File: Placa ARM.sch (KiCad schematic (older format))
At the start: 0 parts

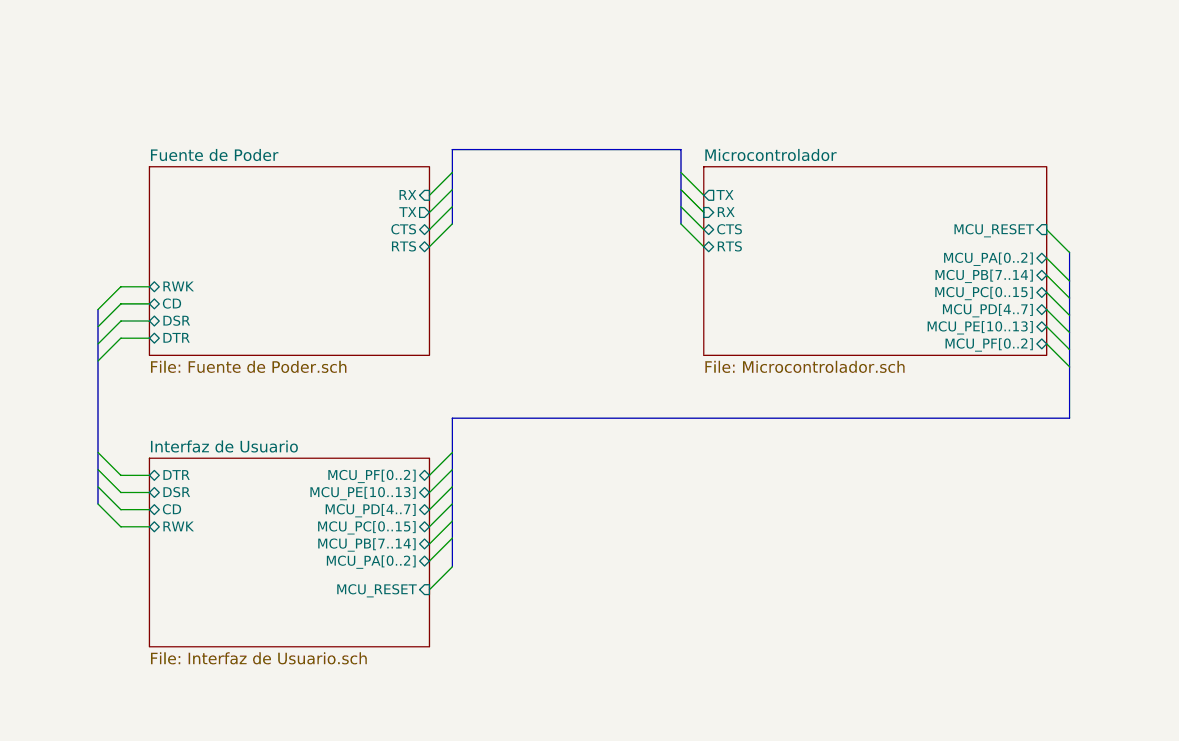
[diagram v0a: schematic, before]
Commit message: Issue #1: Correción de las conexiones Bus
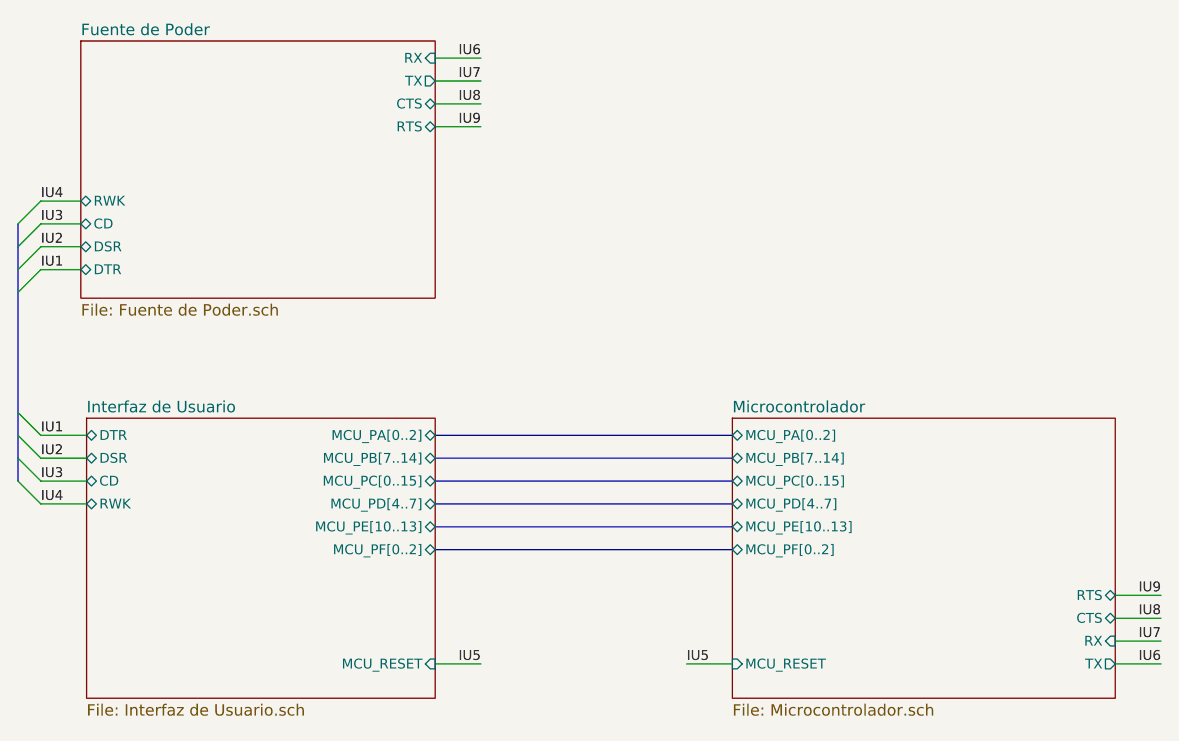
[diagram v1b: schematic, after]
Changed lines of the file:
@@
 $EndDescr
 $Sheet
-S 3950 2700 1225 825
+S 3650 2150 1550 1125
 U 5F4D2198
 F0 "Fuente de Poder" 50
 F1 "Fuente de Poder.sch" 50
-F2 "RX" I R 5175 2825 43
-F3 "TX" O R 5175 2900 43
-F4 "RWK" B L 3950 3225 43
-F5 "CD" B L 3950 3300 43
-F6 "DSR" B L 3950 3375 43
-F7 "DTR" B L 3950 3450 43
-F8 "CTS" B R 5175 2975 43
-F9 "RTS" B R 5175 3050 43
+F2 "RX" I R 5200 2225 43
+F3 "TX" O R 5200 2325 43
+F4 "RWK" B L 3650 2850 43
+F5 "CD" B L 3650 2950 43
+F6 "DSR" B L 3650 3050 43
+F7 "DTR" B L 3650 3150 43
+F8 "CTS" B R 5200 2425 43
+F9 "RTS" B R 5200 2525 43
 $EndSheet
 $Sheet
-S 3950 3975 1225 825
+S 3675 3800 1525 1225
 U 5F4D946F
 F0 "Interfaz de Usuario" 50
 F1 "Interfaz de Usuario.sch" 50
-F2 "RWK" B L 3950 4275 43
-F3 "DTR" B L 3950 4050 43
-F4 "DSR" B L 3950 4125 43
-F5 "CD" B L 3950 4200 43
-F6 "MCU_PA[0..2]" B R 5175 4425 43
-F7 "MCU_PB[7..14]" B R 5175 4350 43
-F8 "MCU_PE[10..13]" B R 5175 4125 43
-F9 "MCU_PC[0..15]" B R 5175 4275 43
-F10 "MCU_PD[4..7]" B R 5175 4200 43
-F11 "MCU_PF[0..2]" B R 5175 4050 43
-F12 "MCU_RESET" I R 5175 4550 43
+F2 "RWK" B L 3675 4175 43
+F3 "DTR" B L 3675 3875 43
+F4 "DSR" B L 3675 3975 43
+F5 "CD" B L 3675 4075 43
+F6 "MCU_PA[0..2]" B R 5200 3875 43
+F7 "MCU_PB[7..14]" B R 5200 3975 43
+F8 "MCU_PE[10..13]" B R 5200 4275 43
+F9 "MCU_PC[0..15]" B R 5200 4075 43
+F10 "MCU_PD[4..7]" B R 5200 4175 43
+F11 "MCU_PF[0..2]" B R 5200 4375 43
+F12 "MCU_RESET" I R 5200 4875 43
 $EndSheet
 $Sheet
-S 6375 2700 1500 825
+S 6500 3800 1675 1225
 U 5F4D1FFB
 F0 "Microcontrolador" 50
 F1 "Microcontrolador.sch" 50
-F2 "MCU_PA[0..2]" B R 7875 3100 43
-F3 "MCU_PB[7..14]" B R 7875 3175 43
-F4 "MCU_PE[10..13]" B R 7875 3400 43
-F5 "MCU_PC[0..15]" B R 7875 3250 43
-F6 "MCU_PD[4..7]" B R 7875 3325 43
-F7 "RX" I L 6375 2900 43
-F8 "TX" O L 6375 2825 43
-F9 "CTS" B L 6375 2975 43
-F10 "RTS" B L 6375 3050 43
-F11 "MCU_PF[0..2]" B R 7875 3475 43
-F12 "MCU_RESET" I R 7875 2975 43
+F2 "MCU_PA[0..2]" B L 6500 3875 43
+F3 "MCU_PB[7..14]" B L 6500 3975 43
+F4 "MCU_PE[10..13]" B L 6500 4275 43
+F5 "MCU_PC[0..15]" B L 6500 4075 43
+F6 "MCU_PD[4..7]" B L 6500 4175 43
+F7 "RX" I R 8175 4775 43
+F8 "TX" O R 8175 4875 43
+F9 "CTS" B R 8175 4675 43
+F10 "RTS" B R 8175 4575 43
+F11 "MCU_PF[0..2]" B L 6500 4375 43
+F12 "MCU_RESET" I L 6500 4875 43
 $EndSheet
 Entry Wire Line
-	3725 3325 3825 3225
+	3375 3150 3475 3050
 Entry Wire Line
-	3725 3400 3825 3300
+	3375 2950 3475 2850
 Entry Wire Line
-	3725 3475 3825 3375
+	3375 3250 3475 3150
 Entry Wire Line
-	3725 3550 3825 3450
+	3375 3050 3475 2950
 Entry Wire Line
-	3725 3950 3825 4050
+	3375 3775 3475 3875
 Entry Wire Line
-	3725 4025 3825 4125
+	3375 3875 3475 3975
 Entry Wire Line
-	3725 4100 3825 4200
+	3375 3975 3475 4075
 Entry Wire Line
-	3725 4175 3825 4275
+	3375 4075 3475 4175
+Text Label 3475 3150 0    43   ~ 0
+IU1
+Text Label 3475 3975 0    43   ~ 0
+IU2
+Text Label 3475 4075 0    43   ~ 0
+IU3
+Text Label 3475 4175 0    43   ~ 0
+IU4
+Text Label 3475 3050 0    43   ~ 0
+IU2
+Text Label 3475 2950 0    43   ~ 0
+IU3
+Text Label 3475 3875 0    43   ~ 0
+IU1
 Wire Wire Line
-	3825 4050 3950 4050
+	3675 3875 3475 3875
 Wire Wire Line
-	3825 4125 3950 4125
+	3675 3975 3475 3975
 Wire Wire Line
-	3825 4200 3950 4200
+	3675 4075 3475 4075
 Wire Wire Line
-	3825 4275 3950 4275
+	3675 4175 3475 4175
 Wire Wire Line
-	3825 3225 3950 3225
+	3475 2850 3650 2850
 Wire Wire Line
-	3825 3300 3950 3300
+	3475 2950 3650 2950
 Wire Wire Line
-	3825 3375 3950 3375
+	3475 3050 3650 3050
 Wire Wire Line
-	3825 3450 3950 3450
-Entry Wire Line
-	6275 2725 6375 2825
-Entry Wire Line
-	6275 2800 6375 2900
-Entry Wire Line
-	6275 2875 6375 2975
-Entry Wire Line
-	6275 2950 6375 3050
-Entry Wire Line
-	5175 2825 5275 2725
-Entry Wire Line
-	5175 2900 5275 2800
-Entry Wire Line
-	5175 2975 5275 2875
-Entry Wire Line
-	5175 3050 5275 2950
+	3475 3150 3650 3150
+Text Label 3475 2850 0    43   ~ 0
+IU4
+Wire Wire Line
+	5200 4875 5400 4875
+Text Label 5400 4875 2    43   ~ 0
+IU5
+Wire Wire Line
+	6500 4875 6300 4875
+Text Label 6300 4875 0    43   ~ 0
+IU5
+Wire Wire Line
+	5200 2225 5400 2225
+Wire Wire Line
+	5200 2325 5400 2325
+Wire Wire Line
+	5200 2425 5400 2425
+Wire Wire Line
+	5200 2525 5400 2525
+Text Label 5400 2225 2    43   ~ 0
+IU6
+Text Label 5400 2325 2    43   ~ 0
+IU7
+Text Label 5400 2425 2    43   ~ 0
+IU8
+Text Label 5400 2525 2    43   ~ 0
+IU9
+Wire Wire Line
+	8175 4575 8375 4575
+Wire Wire Line
+	8175 4675 8375 4675
+Wire Wire Line
+	8175 4775 8375 4775
+Wire Wire Line
+	8175 4875 8375 4875
+Text Label 8375 4775 2    43   ~ 0
+IU7
+Text Label 8375 4675 2    43   ~ 0
+IU8
+Text Label 8375 4575 2    43   ~ 0
+IU9
+Text Label 8375 4875 2    43   ~ 0
+IU6
 Wire Bus Line
-	6275 2625 5275 2625
-Entry Wire Line
-	5175 4050 5275 3950
-Entry Wire Line
-	5175 4125 5275 4025
-Entry Wire Line
-	5175 4200 5275 4100
-Entry Wire Line
-	5175 4275 5275 4175
-Entry Wire Line
-	5175 4350 5275 4250
-Entry Wire Line
-	5175 4425 5275 4325
-Entry Wire Line
-	7875 3100 7975 3200
-Entry Wire Line
-	7875 3175 7975 3275
-Entry Wire Line
-	7875 3250 7975 3350
-Entry Wire Line
-	7875 3325 7975 3425
-Entry Wire Line
-	7875 3400 7975 3500
-Entry Wire Line
-	7875 3475 7975 3575
+	5200 3875 6500 3875
 Wire Bus Line
-	7975 3800 5275 3800
-Entry Wire Line
-	7875 2975 7975 3075
-Entry Wire Line
-	5175 4550 5275 4450
+	6500 3975 5200 3975
 Wire Bus Line
-	6275 2625 6275 2950
+	5200 4075 6500 4075
 Wire Bus Line
-	5275 2625 5275 2950
+	6500 4175 5200 4175
 Wire Bus Line
-	3725 3325 3725 4175
+	5200 4275 6500 4275
 Wire Bus Line
-	5275 3800 5275 4450
+	6500 4375 5200 4375
 Wire Bus Line
-	7975 3075 7975 3800
+	3375 2950 3375 4075
 $EndSCHEMATC

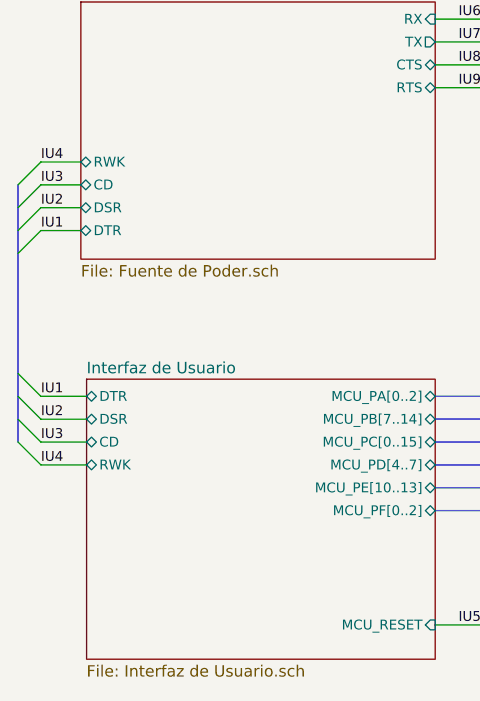
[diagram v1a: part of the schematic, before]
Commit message: Issue #1: Cambio de conector USB-UART
Se agrega un conector para todos los pines UART ofrecidos por el IC
XR21B1411 de Maxlinear.
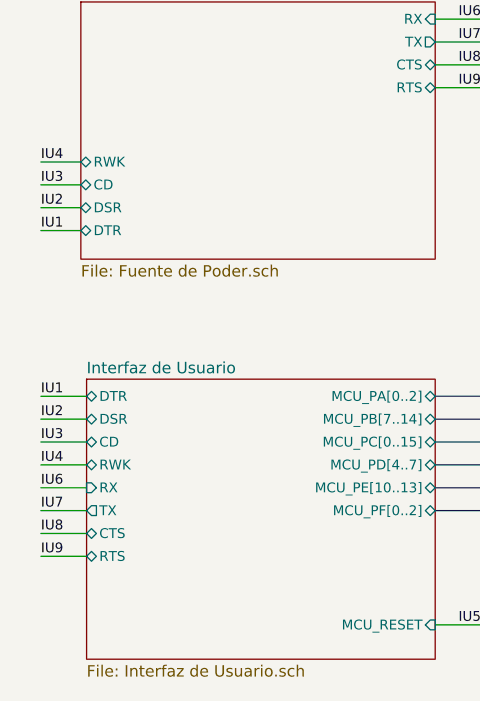
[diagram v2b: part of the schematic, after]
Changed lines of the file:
@@
 F11 "MCU_PF[0..2]" B R 5200 4375 43
 F12 "MCU_RESET" I R 5200 4875 43
+F13 "RX" I L 3675 4275 43
+F14 "TX" O L 3675 4375 43
+F15 "CTS" B L 3675 4475 43
+F16 "RTS" B L 3675 4575 43
 $EndSheet
 $Sheet
@@
 F12 "MCU_RESET" I L 6500 4875 43
 $EndSheet
-Entry Wire Line
-	3375 3150 3475 3050
-Entry Wire Line
-	3375 2950 3475 2850
-Entry Wire Line
-	3375 3250 3475 3150
-Entry Wire Line
-	3375 3050 3475 2950
-Entry Wire Line
-	3375 3775 3475 3875
-Entry Wire Line
-	3375 3875 3475 3975
-Entry Wire Line
-	3375 3975 3475 4075
-Entry Wire Line
-	3375 4075 3475 4175
 Text Label 3475 3150 0    43   ~ 0
 IU1
@@
 Wire Bus Line
 	6500 4375 5200 4375
-Wire Bus Line
-	3375 2950 3375 4075
+Wire Wire Line
+	3675 4275 3475 4275
+Wire Wire Line
+	3675 4375 3475 4375
+Wire Wire Line
+	3675 4475 3475 4475
+Wire Wire Line
+	3675 4575 3475 4575
+Text Label 3475 4275 0    43   ~ 0
+IU6
+Text Label 3475 4375 0    43   ~ 0
+IU7
+Text Label 3475 4475 0    43   ~ 0
+IU8
+Text Label 3475 4575 0    43   ~ 0
+IU9
 $EndSCHEMATC

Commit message: Issue #2: PCB lista para primera prueba de concepto
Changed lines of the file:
@@
 $EndDescr
-$Sheet
-S 3650 2150 1550 1125
-U 5F4D2198
-F0 "Fuente de Poder" 50
-F1 "Fuente de Poder.sch" 50
-F2 "RX" I R 5200 2225 43
-F3 "TX" O R 5200 2325 43
-F4 "RWK" B L 3650 2850 43
-F5 "CD" B L 3650 2950 43
-F6 "DSR" B L 3650 3050 43
-F7 "DTR" B L 3650 3150 43
-F8 "CTS" B R 5200 2425 43
-F9 "RTS" B R 5200 2525 43
-$EndSheet
-$Sheet
-S 3675 3800 1525 1225
-U 5F4D946F
-F0 "Interfaz de Usuario" 50
-F1 "Interfaz de Usuario.sch" 50
-F2 "RWK" B L 3675 4175 43
-F3 "DTR" B L 3675 3875 43
-F4 "DSR" B L 3675 3975 43
-F5 "CD" B L 3675 4075 43
-F6 "MCU_PA[0..2]" B R 5200 3875 43
-F7 "MCU_PB[7..14]" B R 5200 3975 43
-F8 "MCU_PE[10..13]" B R 5200 4275 43
-F9 "MCU_PC[0..15]" B R 5200 4075 43
-F10 "MCU_PD[4..7]" B R 5200 4175 43
-F11 "MCU_PF[0..2]" B R 5200 4375 43
-F12 "MCU_RESET" I R 5200 4875 43
-F13 "RX" I L 3675 4275 43
-F14 "TX" O L 3675 4375 43
-F15 "CTS" B L 3675 4475 43
-F16 "RTS" B L 3675 4575 43
-$EndSheet
 $Sheet
 S 6500 3800 1675 1225
@@
 F12 "MCU_RESET" I L 6500 4875 43
 $EndSheet
-Text Label 3475 3150 0    43   ~ 0
-IU1
-Text Label 3475 3975 0    43   ~ 0
-IU2
-Text Label 3475 4075 0    43   ~ 0
-IU3
-Text Label 3475 4175 0    43   ~ 0
-IU4
-Text Label 3475 3050 0    43   ~ 0
-IU2
-Text Label 3475 2950 0    43   ~ 0
-IU3
-Text Label 3475 3875 0    43   ~ 0
-IU1
-Wire Wire Line
-	3675 3875 3475 3875
-Wire Wire Line
-	3675 3975 3475 3975
-Wire Wire Line
-	3675 4075 3475 4075
-Wire Wire Line
-	3675 4175 3475 4175
-Wire Wire Line
-	3475 2850 3650 2850
-Wire Wire Line
-	3475 2950 3650 2950
-Wire Wire Line
-	3475 3050 3650 3050
-Wire Wire Line
-	3475 3150 3650 3150
-Text Label 3475 2850 0    43   ~ 0
-IU4
 Wire Wire Line
 	5200 4875 5400 4875
@@
 Wire Bus Line
 	6500 4375 5200 4375
+$Sheet
+S 3650 2150 1550 1125
+U 5F4D2198
+F0 "Fuente de Poder" 50
+F1 "Fuente de Poder.sch" 50
+F2 "RX" I R 5200 2225 43
+F3 "TX" O R 5200 2325 43
+F4 "CTS" B R 5200 2425 43
+F5 "RTS" B R 5200 2525 43
+$EndSheet
+Text Label 3475 4575 0    43   ~ 0
+IU9
+Text Label 3475 4475 0    43   ~ 0
+IU8
+Text Label 3475 4375 0    43   ~ 0
+IU7
+Text Label 3475 4275 0    43   ~ 0
+IU6
 Wire Wire Line
-	3675 4275 3475 4275
+	3675 4575 3475 4575
+Wire Wire Line
+	3675 4475 3475 4475
 Wire Wire Line
 	3675 4375 3475 4375
 Wire Wire Line
-	3675 4475 3475 4475
-Wire Wire Line
-	3675 4575 3475 4575
-Text Label 3475 4275 0    43   ~ 0
-IU6
-Text Label 3475 4375 0    43   ~ 0
-IU7
-Text Label 3475 4475 0    43   ~ 0
-IU8
-Text Label 3475 4575 0    43   ~ 0
-IU9
+	3675 4275 3475 4275
+$Sheet
+S 3675 3800 1525 1225
+U 5F4D946F
+F0 "Interfaz de Usuario" 50
+F1 "Interfaz de Usuario.sch" 50
+F2 "MCU_PA[0..2]" B R 5200 3875 43
+F3 "MCU_PB[7..14]" B R 5200 3975 43
+F4 "MCU_PE[10..13]" B R 5200 4275 43
+F5 "MCU_PC[0..15]" B R 5200 4075 43
+F6 "MCU_PD[4..7]" B R 5200 4175 43
+F7 "MCU_PF[0..2]" B R 5200 4375 43
+F8 "MCU_RESET" I R 5200 4875 43
+F9 "RX" I L 3675 4275 43
+F10 "TX" O L 3675 4375 43
+F11 "CTS" B L 3675 4475 43
+F12 "RTS" B L 3675 4575 43
+$EndSheet
 $EndSCHEMATC
